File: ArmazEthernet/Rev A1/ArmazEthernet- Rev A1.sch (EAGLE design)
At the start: 62 parts, among them U1 LAN9303-ABZJ, U2 LAN8710AI-EZK, U3 LP2992IM5-3.3, X10 85505-5113, X8 87832-26

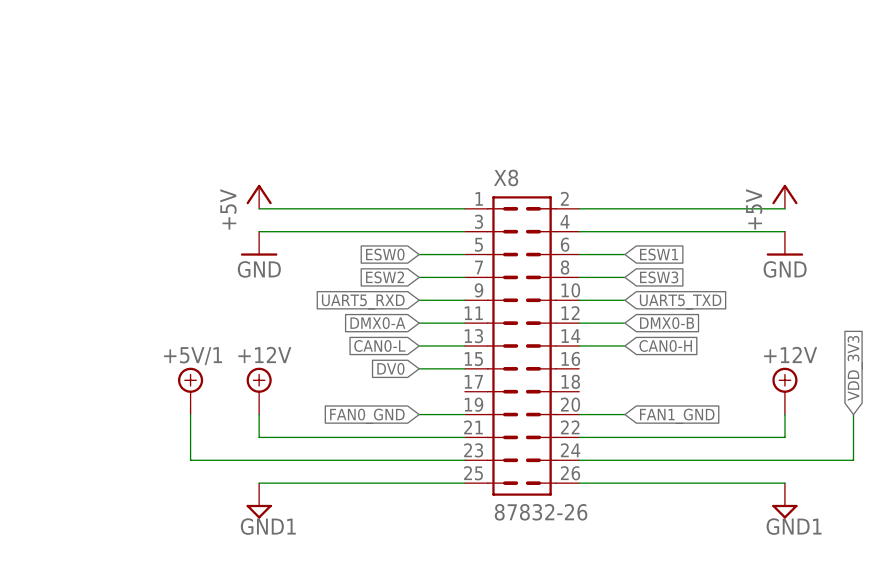
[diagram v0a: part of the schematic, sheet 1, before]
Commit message: Added missing lib: atmel.lbr Provides ATMega328
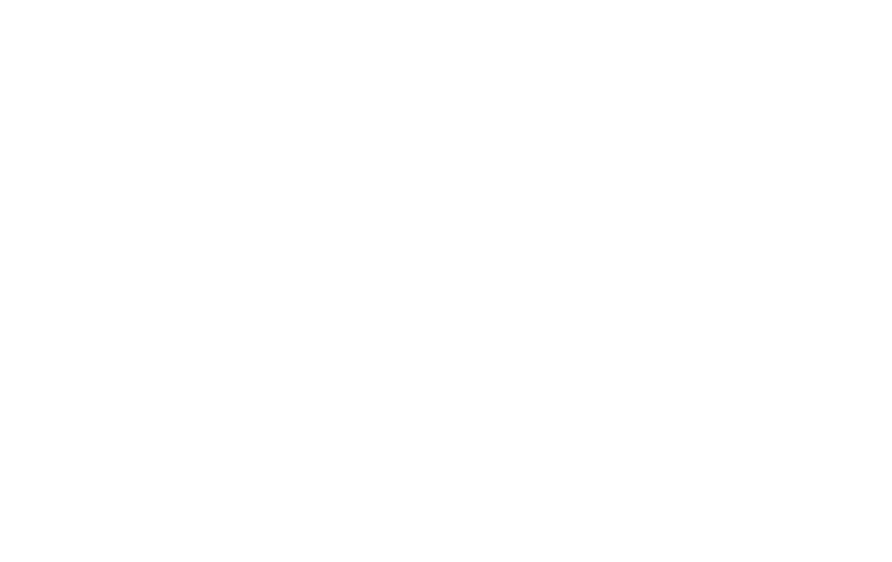
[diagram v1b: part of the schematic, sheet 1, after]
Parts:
- removed X8: 87832-26, con-molex:87832-26
- C23, C24, C25, C26: device rcl:C-EUC0402 -> rcl:C-EUC0603
- R10, R11, R12, R13, R14, R15, R16, R17, R18, R19, R20, R21, R22, SJ2, SJ3, SJ4, SJ5: device rcl:R-EU_R0402 -> rcl:R-EU_R0603
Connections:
- removed net +12V: X8.21, X8.22
- removed net +5V/1: X8.23
- removed net CAN0-H: X8.14
- removed net CAN0-L: X8.13
- removed net DMX0-A: X8.11
- removed net DMX0-B: X8.12
- removed net DV0: X8.15
- removed net ESW0: X8.5
- removed net ESW1: X8.6
- removed net ESW2: X8.7
- removed net ESW3: X8.8
- removed net FAN0_GND: X8.19
- removed net FAN1_GND: X8.20
- removed net GND1: X8.25, X8.26
- removed net UART5_RXD: X8.9
- removed net UART5_TXD: X8.10
- removed net VDD_3V3: X8.24
- net +5V: no longer X8.1, X8.2
- net GND: no longer X8.3, X8.4
